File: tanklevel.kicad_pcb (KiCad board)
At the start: 4 copper layers, 0 parts

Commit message: feat: Switch back to LAN8720A
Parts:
- added C1: 100n, Capacitor_SMD:C_0603_1608Metric_Pad1.08x0.95mm_HandSolder, F.Cu at (187.5, 76.4)
- added C12: 10u, Capacitor_SMD:C_0805_2012Metric_Pad1.18x1.45mm_HandSolder, F.Cu at (181.5, 54.0)
- added C13: 100n, Capacitor_SMD:C_0603_1608Metric_Pad1.08x0.95mm_HandSolder, F.Cu at (185.0, 53.8)
- added C17: 100n, Capacitor_SMD:C_0603_1608Metric_Pad1.08x0.95mm_HandSolder, F.Cu at (227.3, 68.3)
- added C19: 100n, Capacitor_SMD:C_0603_1608Metric_Pad1.08x0.95mm_HandSolder, F.Cu at (222.0, 69.5)
- added C2: 1u, Capacitor_SMD:C_0805_2012Metric_Pad1.18x1.45mm_HandSolder, F.Cu at (185.2, 77.3)
- added C20: 1u, Capacitor_SMD:C_0603_1608Metric_Pad1.08x0.95mm_HandSolder, F.Cu at (185.1, 57.6)
- added C21: 100n, Capacitor_SMD:C_0603_1608Metric_Pad1.08x0.95mm_HandSolder, F.Cu at (225.9, 59.9)
- added C22: 4u7, Capacitor_SMD:C_1210_3225Metric_Pad1.33x2.70mm_HandSolder, F.Cu at (172.3, 101.3)
- added C23: 10u, Capacitor_SMD:C_1210_3225Metric_Pad1.33x2.70mm_HandSolder, F.Cu at (184.2, 95.8)
- added C24: 100n, Capacitor_SMD:C_0603_1608Metric_Pad1.08x0.95mm_HandSolder, F.Cu at (172.3, 98.2)
- added C25: 100n, Capacitor_SMD:C_0603_1608Metric_Pad1.08x0.95mm_HandSolder, F.Cu at (172.6, 82.5)
- added C26: 10u, Capacitor_SMD:C_0603_1608Metric_Pad1.08x0.95mm_HandSolder, F.Cu at (172.6, 84.3)
- added C27: 10u, Capacitor_SMD:C_0603_1608Metric_Pad1.08x0.95mm_HandSolder, F.Cu at (172.5, 86.1)
- added C28: 470p, Capacitor_SMD:C_0603_1608Metric_Pad1.08x0.95mm_HandSolder, F.Cu at (229.4, 64.6)
- added C29: 1u, Capacitor_SMD:C_0603_1608Metric_Pad1.08x0.95mm_HandSolder, F.Cu at (229.4, 62.9)
- added C3: 4u7, Capacitor_SMD:C_0805_2012Metric_Pad1.18x1.45mm_HandSolder, F.Cu at (183.0, 77.3)
- added C30: 20n, Capacitor_SMD:C_0603_1608Metric_Pad1.08x0.95mm_HandSolder, F.Cu at (223.3, 79.7)
- added C4: 100n, Capacitor_SMD:C_0603_1608Metric_Pad1.08x0.95mm_HandSolder, F.Cu at (194.4, 85.1)
- added C5: 10u, Capacitor_SMD:C_0603_1608Metric_Pad1.08x0.95mm_HandSolder, F.Cu at (196.3, 85.1)
- added C6: 100n, Capacitor_SMD:C_0603_1608Metric_Pad1.08x0.95mm_HandSolder, F.Cu at (196.8, 76.0)
- added C7: 1u, Capacitor_SMD:C_0603_1608Metric_Pad1.08x0.95mm_HandSolder, F.Cu at (220.4, 69.5)
- added C9: 1u, Capacitor_SMD:C_0805_2012Metric_Pad1.18x1.45mm_HandSolder, F.Cu at (194.2, 75.2)
- added D1: BAT54S, Package_TO_SOT_SMD:SOT-23, F.Cu at (198.8, 88.2)
- added D2: SS34, Diode_SMD:D_SMA, F.Cu at (188.0, 88.0)
- added D3: SMF5V0A, Diode_SMD:D_SMF, F.Cu at (206.5, 91.5)
- added D4: SMF24A, Diode_SMD:D_SMF, F.Cu at (187.2, 91.5)
- added F1: 1A, Fuse:Fuse_0603_1608Metric_Pad1.05x0.95mm_HandSolder, F.Cu at (193.8, 90.5)
- added F2: 100mA, Fuse:Fuse_0603_1608Metric_Pad1.05x0.95mm_HandSolder, F.Cu at (205.0, 88.4)
- added FB2: BLM18KG331SH1D, Capacitor_SMD:C_0603_1608Metric_Pad1.08x0.95mm_HandSolder, F.Cu at (217.9, 69.6)
- added J1: RJ45_Amphenol_RJMG1BD3B8K1ANR, Connector_RJ:RJ45_Amphenol_RJMG1BD3B8K1ANR, F.Cu at (218.8, 86.4)
- added J4: WAGO250-204, awesome:WAGO250-204, F.Cu at (186.6, 94.4)
- added L1: L, awesome:RLS-126-R, F.Cu at (178.5, 107.5)
- added PGAIN1: 3k, Potentiometer_THT:Potentiometer_Bourns_3296W_Vertical, F.Cu at (212.0, 101.2)
- added PZERO1: 10k, Potentiometer_THT:Potentiometer_Bourns_3296W_Vertical, F.Cu at (206.0, 101.2)
- added R1: 165R, Resistor_SMD:R_1206_3216Metric_Pad1.30x1.75mm_HandSolder, F.Cu at (204.0, 85.3)
- added R12: 33R, Resistor_SMD:R_0603_1608Metric_Pad0.98x0.95mm_HandSolder, F.Cu at (211.4, 61.8)
- added R13: 10K, Resistor_SMD:R_0603_1608Metric_Pad0.98x0.95mm_HandSolder, F.Cu at (183.4, 55.9)
- added R14: 33R, Resistor_SMD:R_0603_1608Metric_Pad0.98x0.95mm_HandSolder, F.Cu at (208.7, 55.8)
- added R15: 12k4, Resistor_SMD:R_0603_1608Metric_Pad0.98x0.95mm_HandSolder, F.Cu at (191.7, 76.4)
- added R17: 100R, Resistor_SMD:R_0603_1608Metric_Pad0.98x0.95mm_HandSolder, F.Cu at (189.5, 76.4)
- added R18: 10K, Resistor_SMD:R_0603_1608Metric_Pad0.98x0.95mm_HandSolder, F.Cu at (182.8, 62.5)
- added R24: 10K, Resistor_SMD:R_0603_1608Metric_Pad0.98x0.95mm_HandSolder, F.Cu at (182.8, 60.8)
- added R25: 10K, Resistor_SMD:R_0603_1608Metric_Pad0.98x0.95mm_HandSolder, F.Cu at (212.4, 53.6)
- added R26: 10K, Resistor_SMD:R_0603_1608Metric_Pad0.98x0.95mm_HandSolder, F.Cu at (178.1, 69.4)
- added R27: 100R, Resistor_SMD:R_0603_1608Metric_Pad0.98x0.95mm_HandSolder, F.Cu at (178.1, 72.9)
- added R28: 10K, Resistor_SMD:R_0603_1608Metric_Pad0.98x0.95mm_HandSolder, F.Cu at (211.4, 63.4)
- added R29: 100R, Resistor_SMD:R_0603_1608Metric_Pad0.98x0.95mm_HandSolder, F.Cu at (178.1, 71.2)
- added R3: 47R, Resistor_SMD:R_0603_1608Metric_Pad0.98x0.95mm_HandSolder, F.Cu at (199.5, 85.2)
- added R30: 100R, Resistor_SMD:R_0603_1608Metric_Pad0.98x0.95mm_HandSolder, F.Cu at (178.1, 67.8)
- added R31: 100R, Resistor_SMD:R_0603_1608Metric_Pad0.98x0.95mm_HandSolder, F.Cu at (178.1, 66.1)
- added R32: 33R, Resistor_SMD:R_0603_1608Metric_Pad0.98x0.95mm_HandSolder, F.Cu at (211.4, 67.4)
- added R33: 33R, Resistor_SMD:R_0603_1608Metric_Pad0.98x0.95mm_HandSolder, F.Cu at (227.4, 59.9)
- added R34: 33R, Resistor_SMD:R_0603_1608Metric_Pad0.98x0.95mm_HandSolder, F.Cu at (229.0, 59.9)
- added R36: 10K, Resistor_SMD:R_0603_1608Metric_Pad0.98x0.95mm_HandSolder, F.Cu at (223.3, 56.6)
- added R37: 12K1 1%, Resistor_SMD:R_0603_1608Metric_Pad0.98x0.95mm_HandSolder, F.Cu at (227.2, 71.3)
- added R38: 50R, Resistor_SMD:R_0603_1608Metric_Pad0.98x0.95mm_HandSolder, F.Cu at (219.3, 79.6)
- added R39: 50R, Resistor_SMD:R_0603_1608Metric_Pad0.98x0.95mm_HandSolder, F.Cu at (217.3, 79.6)
- added R4: 10K, Resistor_SMD:R_0603_1608Metric_Pad0.98x0.95mm_HandSolder, F.Cu at (185.3, 83.5)
- added R40: 10K, Resistor_SMD:R_0603_1608Metric_Pad0.98x0.95mm_HandSolder, F.Cu at (211.5, 89.3)
- added R41: 50R, Resistor_SMD:R_0603_1608Metric_Pad0.98x0.95mm_HandSolder, F.Cu at (227.2, 79.7)
- added R42: 50R, Resistor_SMD:R_0603_1608Metric_Pad0.98x0.95mm_HandSolder, F.Cu at (225.2, 79.7)
- added R43: 10K, Resistor_SMD:R_0603_1608Metric_Pad0.98x0.95mm_HandSolder, F.Cu at (211.5, 90.9)
- added R44: 1K, Resistor_SMD:R_0603_1608Metric_Pad0.98x0.95mm_HandSolder, F.Cu at (230.4, 79.7)
- added R45: 1K, Resistor_SMD:R_0603_1608Metric_Pad0.98x0.95mm_HandSolder, F.Cu at (232.1, 79.7)
- added R5: 10K, Resistor_SMD:R_0603_1608Metric_Pad0.98x0.95mm_HandSolder, F.Cu at (197.0, 80.2)
- added R6: 10K, Resistor_SMD:R_0603_1608Metric_Pad0.98x0.95mm_HandSolder, F.Cu at (211.4, 65.7)
- added R7: 12k4, Resistor_SMD:R_0603_1608Metric_Pad0.98x0.95mm_HandSolder, F.Cu at (194.0, 79.2)
- added U1: wuerthDebug6, awesome:wuerthDebug6, F.Cu at (174.3, 49.2)
- added U2: MCP6022, Package_SO:SOIC-8_3.9x4.9mm_P1.27mm, F.Cu at (190.1, 82.0)
- added U3: wuerthJTAG, awesome:wuerthJTAG, F.Cu at (171.0, 61.4)
- added U4: R-78E3.3-0.5, Converter_DCDC:Converter_DCDC_RECOM_R-78E-0.5_THT, F.Cu at (176.5, 90.5)
- added U5: LAN8720A, Package_DFN_QFN:QFN-24-1EP_4x4mm_P0.5mm_EP2.6x2.6mm, F.Cu at (223.9, 65.1)
- added U6: ESP32-WROOM-32, awesome:ESP32-WROOM-32, F.Cu at (197.0, 61.5)
- added U7: MCP3221, Package_TO_SOT_SMD:SOT-23-5, F.Cu at (199.6, 76.8)
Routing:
- net VDDA: track 0.00 -> 73.4 mm, vias 0 -> 7
- net /L4: track 0.00 -> 66.2 mm, vias 0 -> 1
- net /L1: track 0.00 -> 62.9 mm, vias 0 -> 1
- net /RXD1: track 0.00 -> 56.7 mm, vias 0 -> 2
- net /CRS: track 0.00 -> 54.2 mm, vias 0 -> 2
- net /RXD0: track 0.00 -> 50.3 mm, vias 0 -> 2
- net /BOOT0: track 0.00 -> 49.0 mm, vias 0 -> 2
- net Net-(PGAIN1-Pad2): track 0.00 -> 45.0 mm, vias 0 -> 1
- net +3.3V: track 0.00 -> 44.1 mm, vias 0 -> 9
- net /SDA: track 0.00 -> 42.3 mm, vias 0 -> 2
- net /RXD: track 0.00 -> 41.8 mm, vias 0 -> 1
- net /SCL: track 0.00 -> 37.4 mm, vias 0 -> 2
- net /TXD: track 0.00 -> 37.0 mm, vias 0 -> 1
- net GND: track 0.00 -> 35.4 mm, vias 0 -> 16
- net /24V: track 0.00 -> 34.5 mm
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- added copper zone on In1.Cu, net +3.3V
- added copper zone on B.Cu, net GND
- added copper zone on F.Cu, net GND
- added copper zone on In2.Cu, net GND
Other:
- board outline added: 70 x 60 mm

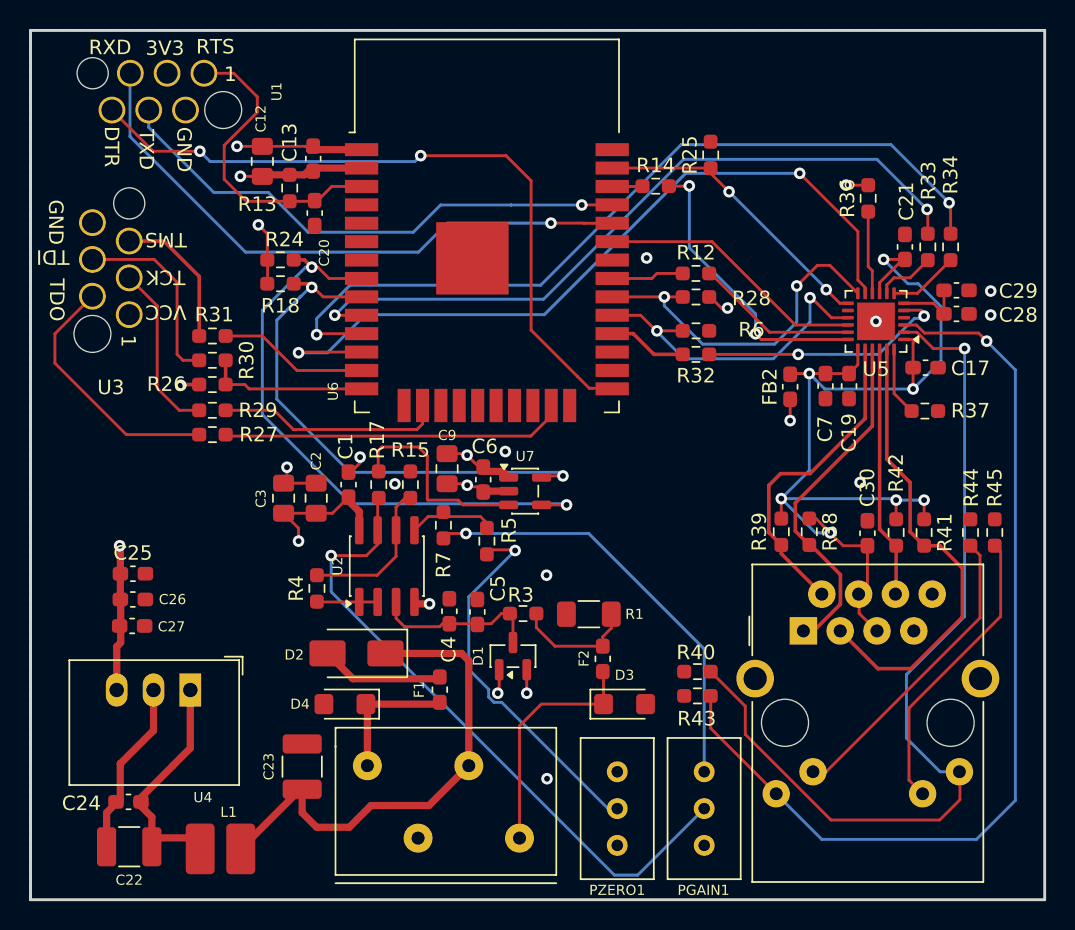
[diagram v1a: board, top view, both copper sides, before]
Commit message: feat: Update to tanklevel v2 pcb
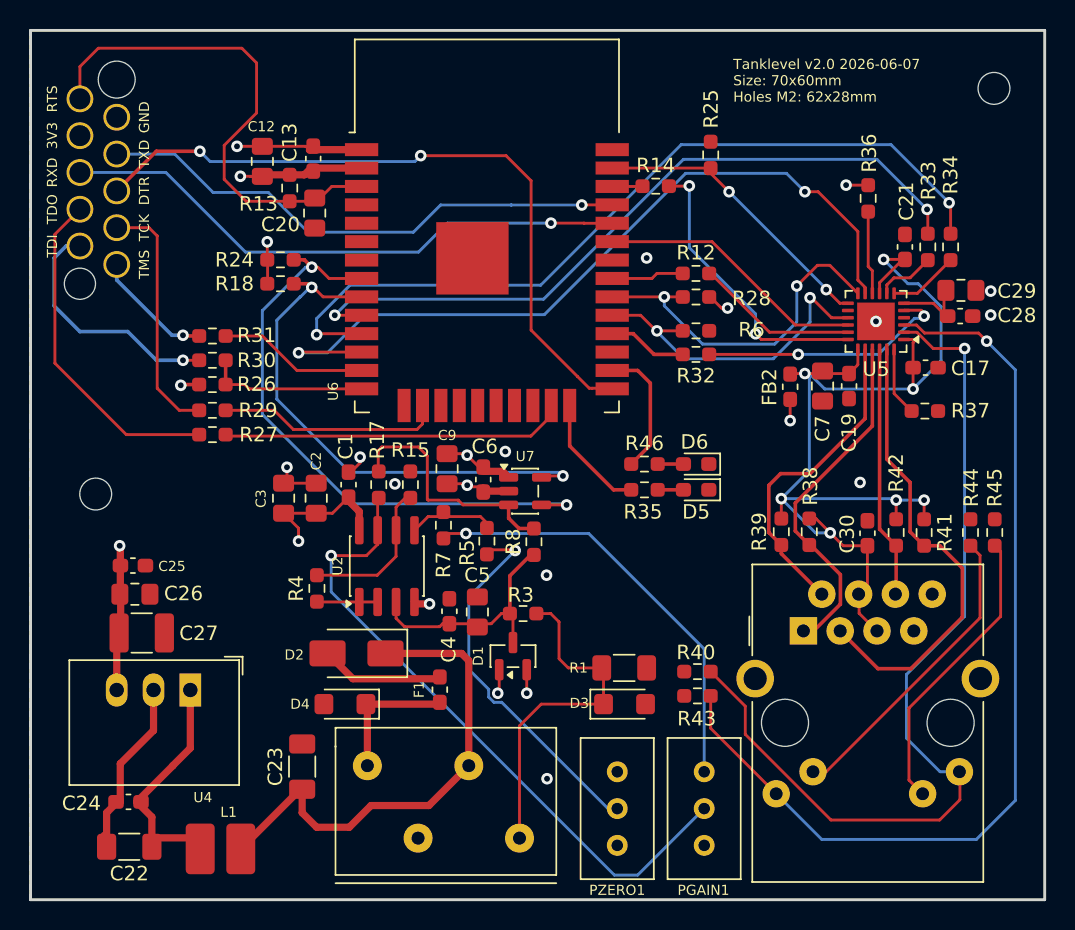
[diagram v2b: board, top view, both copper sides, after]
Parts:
- removed F2: 100mA, Fuse:Fuse_0603_1608Metric_Pad1.05x0.95mm_HandSolder
- removed U1: wuerthDebug6, awesome:wuerthDebug6
- removed U3: wuerthJTAG, awesome:wuerthJTAG
- added D5: LED, LED_SMD:LED_0603_1608Metric_Pad1.05x0.95mm_HandSolder, F.Cu at (211.4, 76.7)
- added D6: LED, LED_SMD:LED_0603_1608Metric_Pad1.05x0.95mm_HandSolder, F.Cu at (211.4, 74.9)
- added H1: MountingHole, MountingHole:MountingHole_2.2mm_M2_DIN965, F.Cu at (232.0, 49.0)
- added H2: MountingHole, MountingHole:MountingHole_2.2mm_M2_DIN965, F.Cu at (170.0, 77.0)
- added R35: 10K, Resistor_SMD:R_0603_1608Metric_Pad0.98x0.95mm_HandSolder, F.Cu at (207.9, 76.7)
- added R46: 10K, Resistor_SMD:R_0603_1608Metric_Pad0.98x0.95mm_HandSolder, F.Cu at (207.9, 74.9)
- added R8: 47R, Resistor_SMD:R_0603_1608Metric_Pad0.98x0.95mm_HandSolder, F.Cu at (200.2, 80.3)
- added U8: wuerthDebug10, awesome:wuerth10, F.Cu at (170.2, 54.8)
- C20, C26, C29, C5, C7: footprint Capacitor_SMD:C_0603_1608Metric_Pad1.08x0.95mm_HandSolder -> Capacitor_SMD:C_0805_2012Metric_Pad1.18x1.45mm_HandSolder
- C22, C23: footprint Capacitor_SMD:C_1210_3225Metric_Pad1.33x2.70mm_HandSolder -> Capacitor_SMD:C_1206_3216Metric_Pad1.33x1.80mm_HandSolder
- C27: value 10u -> 47u; footprint Capacitor_SMD:C_0603_1608Metric_Pad1.08x0.95mm_HandSolder -> Capacitor_SMD:C_1210_3225Metric_Pad1.33x2.70mm_HandSolder
- FB2: footprint Capacitor_SMD:C_0603_1608Metric_Pad1.08x0.95mm_HandSolder -> Inductor_SMD:L_0603_1608Metric_Pad1.05x0.95mm_HandSolder
- R12, R14, R32, R33, R34: value 33R -> 22R
- R38, R39, R41, R42: value 50R -> 51R
- moved R1 4.44 mm to (206.5, 89.0), turned to 0 degrees
- moved C27 0.82 mm to (173.2, 86.6)
- moved C25 0.56 mm to (172.6, 81.9)
- moved C26 0.39 mm to (172.7, 83.9)
- moved C29 0.30 mm to (229.7, 62.9)
- moved C28 0.30 mm to (229.7, 64.7)
- moved C7 0.20 mm to (220.2, 69.5)
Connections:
- R1 pad 1: Net-(F2-Pad2) -> Net-(D3-A1)
- R3 pad 1: Net-(F2-Pad2) -> Net-(D3-A1)
- U6 pad 24: unconnected-(U6-IO2-Pad24) -> Net-(U6-IO2)
- U6 pad 26: unconnected-(U6-IO4-Pad26) -> Net-(U6-IO4)
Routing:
- net /EN: track 21.5 -> 34.9 mm
- net Net-(U6-IO4): track 0.00 -> 9.12 mm
- net Net-(F2-Pad2): track 8.60 -> 0.00 mm
- net Net-(U6-IO2): track 0.00 -> 8.29 mm
- net Net-(D3-A1): track 16.4 -> 24.3 mm
- net Net-(U8-TDO): track 17.7 -> 23.3 mm
- net Net-(U8-TCK): track 11.9 -> 17.1 mm
- net Net-(D1-COM): track 12.0 -> 16.8 mm
- net Net-(U8-TDI): track 13.2 -> 17.0 mm, vias 0 -> 1
- net /ADC_IN: track 14.0 -> 16.9 mm
- net /RXD: track 41.8 -> 39.8 mm
- net Net-(D6-A): track 0.00 -> 1.78 mm
- net Net-(D5-A): track 0.00 -> 1.78 mm
- net Net-(U8-TMS): track 9.95 -> 8.37 mm, vias 0 -> 1
- net +3.3V: track 44.1 -> 42.6 mm
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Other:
- board text added: "Tanklevel v2.0 2026-06-07 Size: 70x60mm Holes M2: 62x28mm"

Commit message: feat: Create fab output
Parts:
- C1, C13, C17, C19, C21, C24, C25, C28, C30, C4, C6: footprint Capacitor_SMD:C_0603_1608Metric_Pad1.08x0.95mm_HandSolder -> Capacitor_SMD:C_0603_1608Metric
- C12, C2, C20, C26, C29, C3, C5, C7, C9: footprint Capacitor_SMD:C_0805_2012Metric_Pad1.18x1.45mm_HandSolder -> Capacitor_SMD:C_0805_2012Metric
- C22, C23: footprint Capacitor_SMD:C_1206_3216Metric_Pad1.33x1.80mm_HandSolder -> Capacitor_SMD:C_1206_3216Metric
- C27: footprint Capacitor_SMD:C_1210_3225Metric_Pad1.33x2.70mm_HandSolder -> Capacitor_SMD:C_1210_3225Metric
- D5, D6: footprint LED_SMD:LED_0603_1608Metric_Pad1.05x0.95mm_HandSolder -> LED_SMD:LED_0603_1608Metric
- F1: footprint Fuse:Fuse_0603_1608Metric_Pad1.05x0.95mm_HandSolder -> Fuse:Fuse_0603_1608Metric
- FB2: footprint Inductor_SMD:L_0603_1608Metric_Pad1.05x0.95mm_HandSolder -> Inductor_SMD:L_0603_1608Metric
- R1: footprint Resistor_SMD:R_1206_3216Metric_Pad1.30x1.75mm_HandSolder -> Resistor_SMD:R_1206_3216Metric
- R12, R13, R14, R15, R17, R18, R24, R25, R26, R27, R28, R29, R3, R30, R31, R32, R33, R34, R35, R36, R37, R38, R39, R4, R40, R41, R42, R43, R44, R45, R46, R5, R6, R7, R8: footprint Resistor_SMD:R_0603_1608Metric_Pad0.98x0.95mm_HandSolder -> Resistor_SMD:R_0603_1608Metric
